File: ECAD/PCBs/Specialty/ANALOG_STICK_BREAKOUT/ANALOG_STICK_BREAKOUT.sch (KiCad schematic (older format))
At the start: 6 parts, among them J1 Conn_01x05

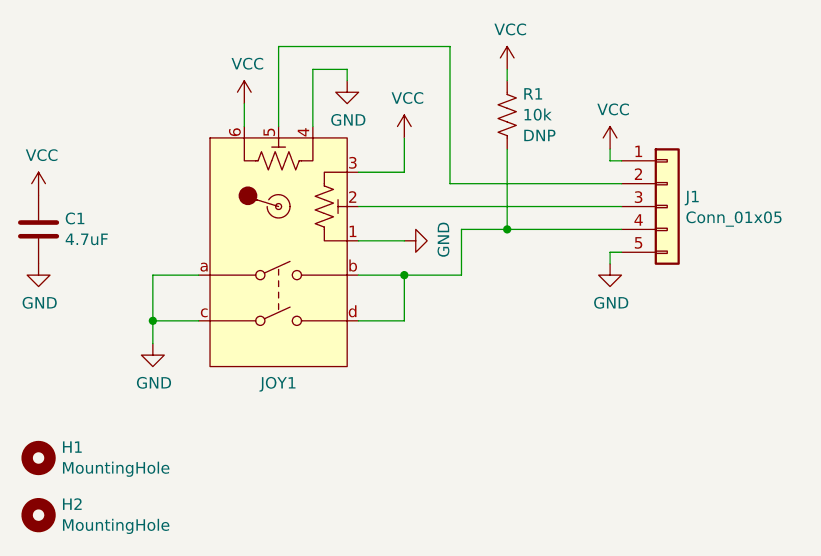
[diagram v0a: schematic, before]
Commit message: Updated all the throttle components to use solder pads attached to the <switch> side components, and changed board shapes created new step models
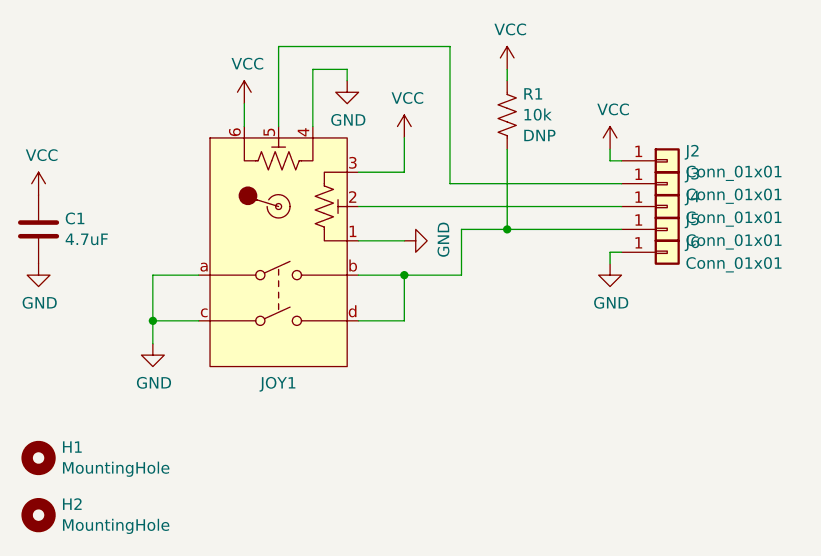
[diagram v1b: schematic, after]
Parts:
- removed J1: Conn_01x05, Connector_JST:JST_PH_B5B-PH-K_1x05_P2.00mm_Vertical, symbol Connector_Generic:Conn_01x05
- added J2, J3, J4, J5, J6: Conn_01x01, KiCAD_Libraries:SolderWirePad_1x01_SMD_2x4mm, symbol Connector_Generic:Conn_01x01
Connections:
- net GND: now also J6.1 (Pin_1)
- net VCC: now also J2.1 (Pin_1)
- net at JOY1.5: now also J3.1 (Pin_1)
- net at JOY1.2: now also J4.1 (Pin_1)
- net at JOY1.b, JOY1.d, R1.2: now also J5.1 (Pin_1)
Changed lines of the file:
@@
-$EndComp
-$Comp
-L Connector_Generic:Conn_01x05 J1
-U 1 1 5ED5CE8A
-P 5100 2500
-F 0 "J1" H 5180 2542 50  0000 L CNN
-F 1 "Conn_01x05" H 5180 2451 50  0000 L CNN
-F 2 "Connector_JST:JST_PH_B5B-PH-K_1x05_P2.00mm_Vertical" H 5100 2500 50  0001 C CNN
-F 3 "~" H 5100 2500 50  0001 C CNN
-	1    5100 2500
-	1    0    0    -1
 $EndComp
 $Comp
@@
 	1    0    0    -1
 $EndComp
+$Comp
+L Connector_Generic:Conn_01x01 J2
+U 1 1 5EDB9436
+P 5100 2300
+F 0 "J2" H 5180 2342 50  0000 L CNN
+F 1 "Conn_01x01" H 5180 2251 50  0000 L CNN
+F 2 "KiCAD_Libraries:SolderWirePad_1x01_SMD_2x4mm" H 5100 2300 50  0001 C CNN
+F 3 "~" H 5100 2300 50  0001 C CNN
+	1    5100 2300
+	1    0    0    -1
+$EndComp
+$Comp
+L Connector_Generic:Conn_01x01 J3
+U 1 1 5EDBA3C5
+P 5100 2400
+F 0 "J3" H 5180 2442 50  0000 L CNN
+F 1 "Conn_01x01" H 5180 2351 50  0000 L CNN
+F 2 "KiCAD_Libraries:SolderWirePad_1x01_SMD_2x4mm" H 5100 2400 50  0001 C CNN
+F 3 "~" H 5100 2400 50  0001 C CNN
+	1    5100 2400
+	1    0    0    -1
+$EndComp
+$Comp
+L Connector_Generic:Conn_01x01 J4
+U 1 1 5EDBAAA8
+P 5100 2500
+F 0 "J4" H 5180 2542 50  0000 L CNN
+F 1 "Conn_01x01" H 5180 2451 50  0000 L CNN
+F 2 "KiCAD_Libraries:SolderWirePad_1x01_SMD_2x4mm" H 5100 2500 50  0001 C CNN
+F 3 "~" H 5100 2500 50  0001 C CNN
+	1    5100 2500
+	1    0    0    -1
+$EndComp
+$Comp
+L Connector_Generic:Conn_01x01 J5
+U 1 1 5EDBB222
+P 5100 2600
+F 0 "J5" H 5180 2642 50  0000 L CNN
+F 1 "Conn_01x01" H 5180 2551 50  0000 L CNN
+F 2 "KiCAD_Libraries:SolderWirePad_1x01_SMD_2x4mm" H 5100 2600 50  0001 C CNN
+F 3 "~" H 5100 2600 50  0001 C CNN
+	1    5100 2600
+	1    0    0    -1
+$EndComp
+$Comp
+L Connector_Generic:Conn_01x01 J6
+U 1 1 5EDBB5F1
+P 5100 2700
+F 0 "J6" H 5180 2742 50  0000 L CNN
+F 1 "Conn_01x01" H 5180 2651 50  0000 L CNN
+F 2 "KiCAD_Libraries:SolderWirePad_1x01_SMD_2x4mm" H 5100 2700 50  0001 C CNN
+F 3 "~" H 5100 2700 50  0001 C CNN
+	1    5100 2700
+	1    0    0    -1
+$EndComp

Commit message: Inner Grip Complete (sans ANT ELEV pot nut)
Inner Grip PCBs and MCAD complete except for TODO item of ANT ELEV POT nut cutout in the ANT ELEV plate. (Waiting on info on nut size from manufacturer.)
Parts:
- C1: LCSC (none) -> C29823
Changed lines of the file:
@@
 F 1 "4.7uF" H 2465 2555 50  0000 L CNN
 F 2 "Capacitor_SMD:C_1206_3216Metric" H 2388 2450 50  0001 C CNN
-F 3 "~" H 2350 2600 50  0001 C CNN
+F 3 "https://datasheet.lcsc.com/lcsc/1811091112_FH-Guangdong-Fenghua-Advanced-Tech-1206B475K500NT_C29823.pdf" H 2350 2600 50  0001 C CNN
+F 4 "C29823" H 2350 2600 50  0001 C CNN "LCSC"
 	1    2350 2600
 	1    0    0    -1
